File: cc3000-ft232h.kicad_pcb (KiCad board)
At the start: 2 copper layers, 50 x 50 mm, 64 parts, among them CON1 USB-MINI-B, IC1 V_REG_LM1117SOT223, P1 CONN_4X2, P2 CONN_8, P3 CONN_13, P4 CONN_13, P5 CONN_4, P6 CONN_1, P7 CONN_6, P8 CONN_8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

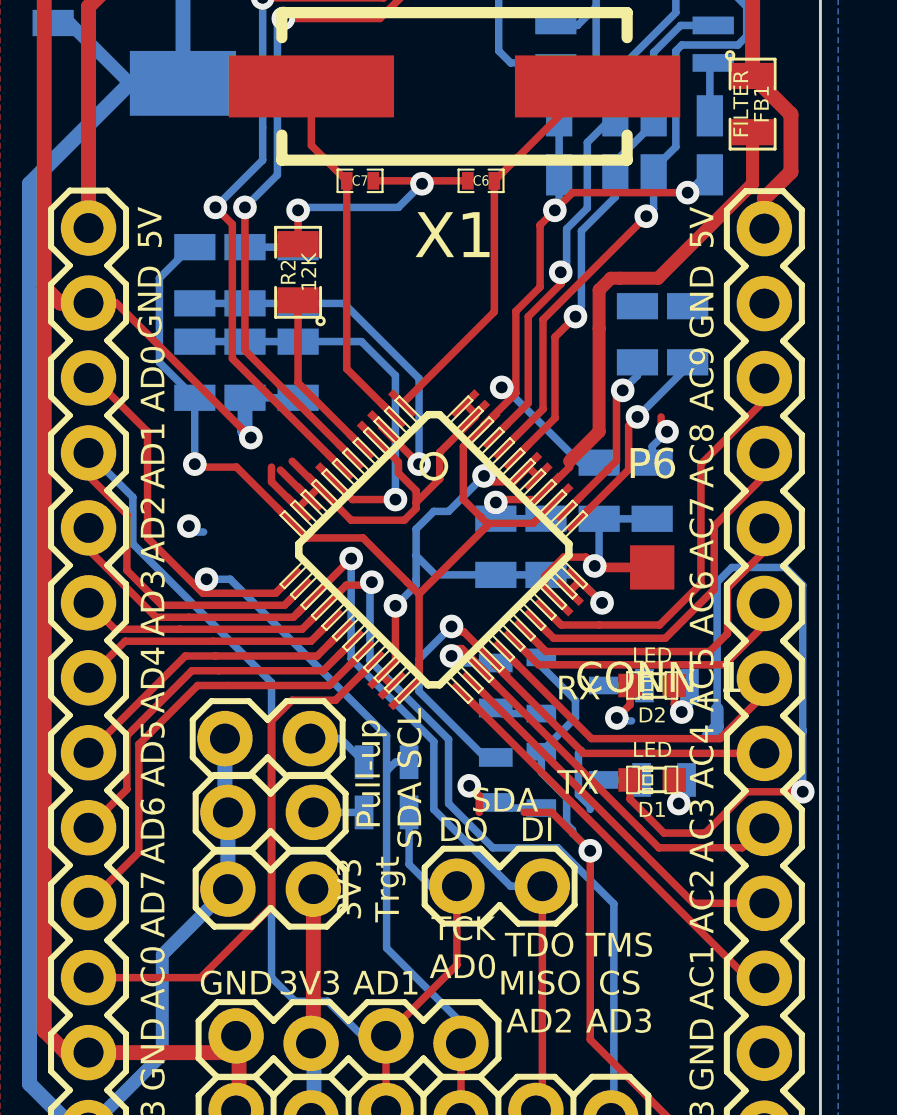
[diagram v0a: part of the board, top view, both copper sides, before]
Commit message: decoupling caps , silk screen modified
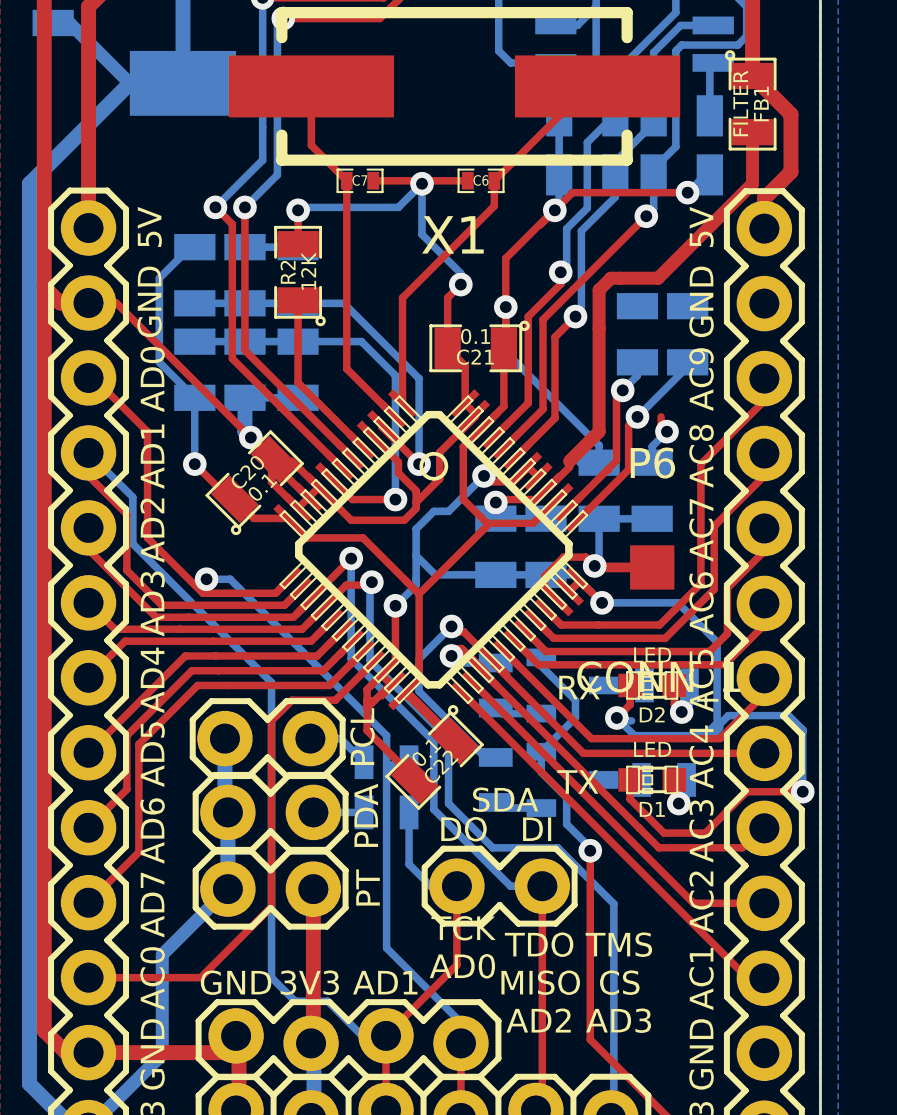
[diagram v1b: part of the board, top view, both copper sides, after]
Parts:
- added C20: 0.1, SM0805, F.Cu at (155.8, 96.5)
- added C21: 0.1, SM0805, F.Cu at (163.3, 92.1)
- added C22: 0.1, SM0805, F.Cu at (161.9, 106.0)
- R1: value 12K -> 10k
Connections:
- CON1 pad 4: (no net) -> N-0000067
- U2 pad 2: (no net) -> N-000006
- U2 pad 24: (no net) -> N-000005
- U2 pad 3: (no net) -> N-0000019
- U2 pad 4: (no net) -> N-0000011
- U2 pad 6: (no net) -> N-000002
- U2 pad 8: (no net) -> N-000003
- U5 pad 7: (no net) -> N-0000065
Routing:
- net GND: track 422.6 -> 439.0 mm, vias 55 -> 56
- net /ft232h/VCC3V3: track 65.4 -> 71.0 mm
- net (no net): track 2.93 -> 0.00 mm, vias 1 -> 0
- net +3.3V: track 168.5 -> 165.8 mm
- net N-0000045: track 3.80 -> 1.62 mm, vias 1 -> 0
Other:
- board text added: "PCL"
- board text added: "PCL: Clock PDA: Data"
- board text added: "PDA"
- board text added: "PT"
- board text added: "PT:Power Target"
- board text added: "i2c Pullup:"
- board text removed: "3V3 Trgt"
- board text removed: "Pull-up"
- board text removed: "SCL"

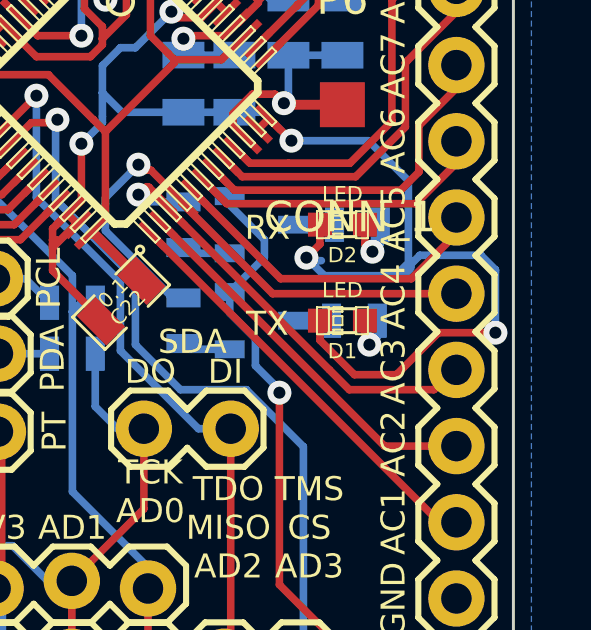
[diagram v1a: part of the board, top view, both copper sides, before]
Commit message: via replaced
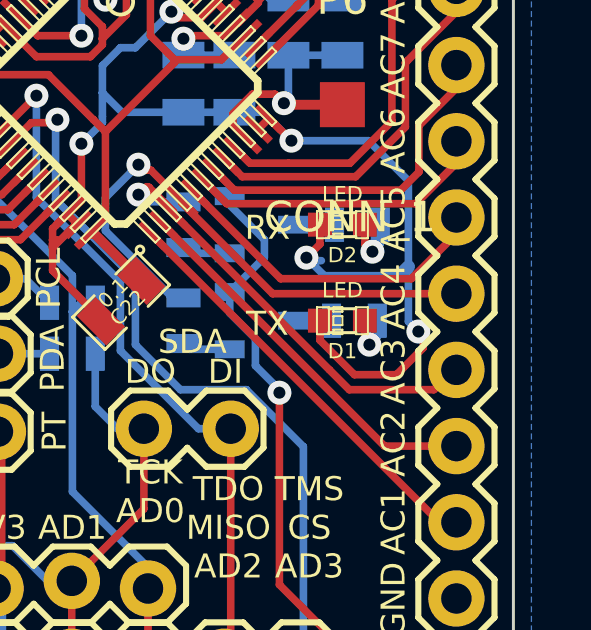
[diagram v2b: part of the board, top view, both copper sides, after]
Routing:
- net GND: track 439.0 -> 433.8 mm
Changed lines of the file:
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@@
     (links 238)
     (no_connects 2)
-    (area 124.949999 69.949999 175.050001 120.050001)
+    (area 123.238 68.101556 177.7482 129.7)
     (thickness 1.6)
     (drawings 75)
-    (tracks 1070)
+    (tracks 1067)
     (zones 0)
     (modules 67)
@@
   )
   (setup
-    (last_trace_width 0.33)
+    (last_trace_width 0.254)
     (user_trace_width 0.33)
     (user_trace_width 0.44)
@@
   (segment (start 165.821136 96.778864) (end 166.5 96.1) (width 0.254) (layer F.Cu) (net 37))
   (segment (start 172.7 85.2) (end 172.7 84.7525) (width 0.44) (layer F.Cu) (net 37))
+  (segment (start 171.9945 107.6055) (end 171.9945 107.2245) (width 0.254) (layer F.Cu) (net 38))
+  (segment (start 171.5 106.73) (end 171.5 104.9) (width 0.254) (layer B.Cu) (net 38))
+  (segment (start 171.831 107.061) (end 171.5 106.73) (width 0.254) (layer B.Cu) (net 38))
+  (via (at 171.831 107.061) (size 0.8) (layers F.Cu B.Cu) (net 38))
+  (segment (start 171.9945 107.2245) (end 171.831 107.061) (width 0.254) (layer F.Cu) (net 38))
   (segment (start 160.484712 103.494299) (end 160.411701 103.494299) (width 0.254) (layer F.Cu) (net 38))
   (segment (start 159.766 104.013) (end 159.639 104.013) (width 0.254) (layer F.Cu) (net 38))
@@
   (segment (start 156.446481 95.846481) (end 155.7 95.1) (width 0.254) (layer F.Cu) (net 38))
   (segment (start 167.6 100.7) (end 170.169 100.7) (width 0.254) (layer B.Cu) (net 38))
-  (segment (start 171.5 102.031) (end 171.5 104.9) (width 0.254) (layer B.Cu) (net 38))
   (segment (start 170.169 100.7) (end 171.5 102.031) (width 0.254) (layer B.Cu) (net 38))
+  (segment (start 171.5 102.031) (end 171.5 104.9) (width 0.254) (layer B.Cu) (net 38))
   (segment (start 171.2 105.2) (end 168.7 105.2) (width 0.254) (layer B.Cu) (net 38))
-  (segment (start 168.7 105.2) (end 168.1 104.6) (width 0.254) (layer B.Cu) (net 38))
   (segment (start 171.5 104.9) (end 171.2 105.2) (width 0.44) (layer B.Cu) (net 38))
-  (segment (start 171.879 104.521) (end 171.5 104.9) (width 0.254) (layer B.Cu) (net 38))
-  (segment (start 173.863 104.521) (end 173.921 104.521) (width 0.254) (layer B.Cu) (net 38))
-  (segment (start 174.4 105) (end 173.921 104.521) (width 0.254) (layer B.Cu) (net 38))
-  (segment (start 173.863 104.521) (end 171.879 104.521) (width 0.254) (layer B.Cu) (net 38))
+  (segment (start 168.7 105.2) (end 168.1 104.6) (width 0.254) (layer B.Cu) (net 38))
   (segment (start 169.6 94.7) (end 169.6 94.4) (width 0.254) (layer F.Cu) (net 38))
   (segment (start 157.63089 97.13089) (end 156.7 96.2) (width 0.254) (layer F.Cu) (net 38))
@@
   (segment (start 168.1 104.6) (end 168.2 104.7) (width 0.254) (layer B.Cu) (net 38))
   (segment (start 168.5507 106.7) (end 168.5507 107.3507) (width 0.254) (layer F.Cu) (net 38))
-  (segment (start 174.4 105) (end 174.4 105.1) (width 0.254) (layer B.Cu) (net 38))
-  (segment (start 174.4 107.1) (end 174.4 105) (width 0.254) (layer B.Cu) (net 38))
-  (via (at 174.4 107.1) (size 0.8) (layers F.Cu B.Cu) (net 38))
-  (segment (start 172.5 107.1) (end 174.4 107.1) (width 0.254) (layer F.Cu) (net 38))
-  (segment (start 171.1 108.5) (end 172.5 107.1) (width 0.254) (layer F.Cu) (net 38))
+  (segment (start 171.1 108.5) (end 171.9945 107.6055) (width 0.254) (layer F.Cu) (net 38))
   (segment (start 169.7 108.5) (end 171.1 108.5) (width 0.254) (layer F.Cu) (net 38))
   (segment (start 168.5507 107.3507) (end 169.7 108.5) (width 0.254) (layer F.Cu) (net 38))
